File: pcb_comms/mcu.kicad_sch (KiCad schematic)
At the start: 34 parts, among them U3 STM32WLE5CCU6, Y1 32.768KHz, Y2 32MHz

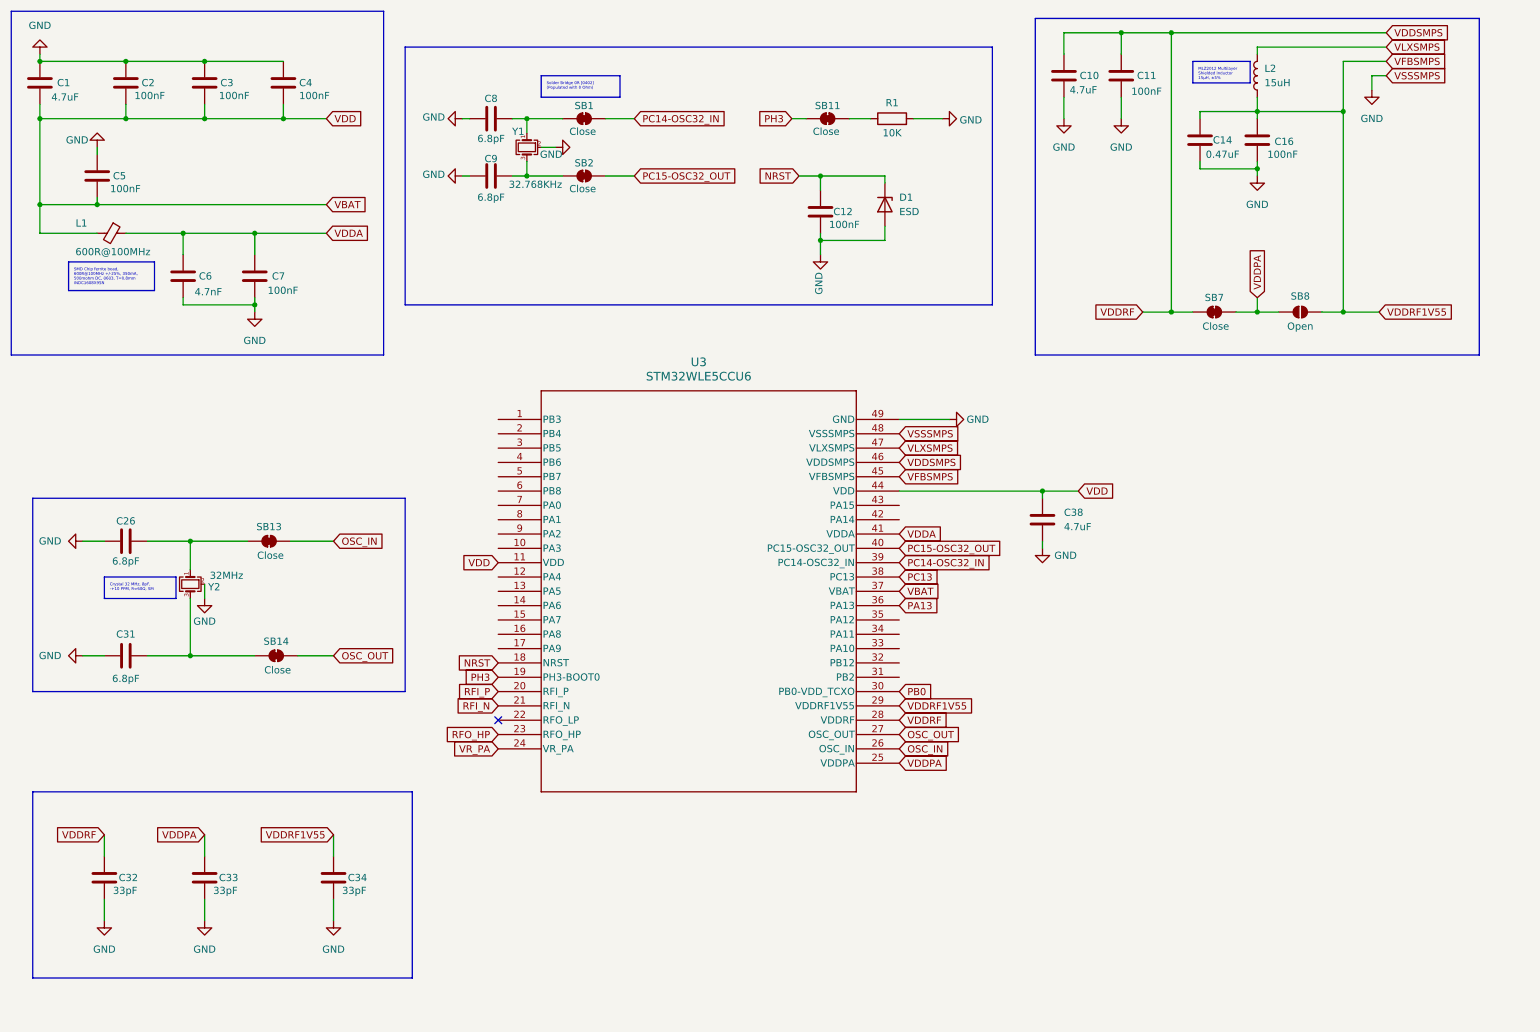
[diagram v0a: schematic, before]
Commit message: Add usb and gps
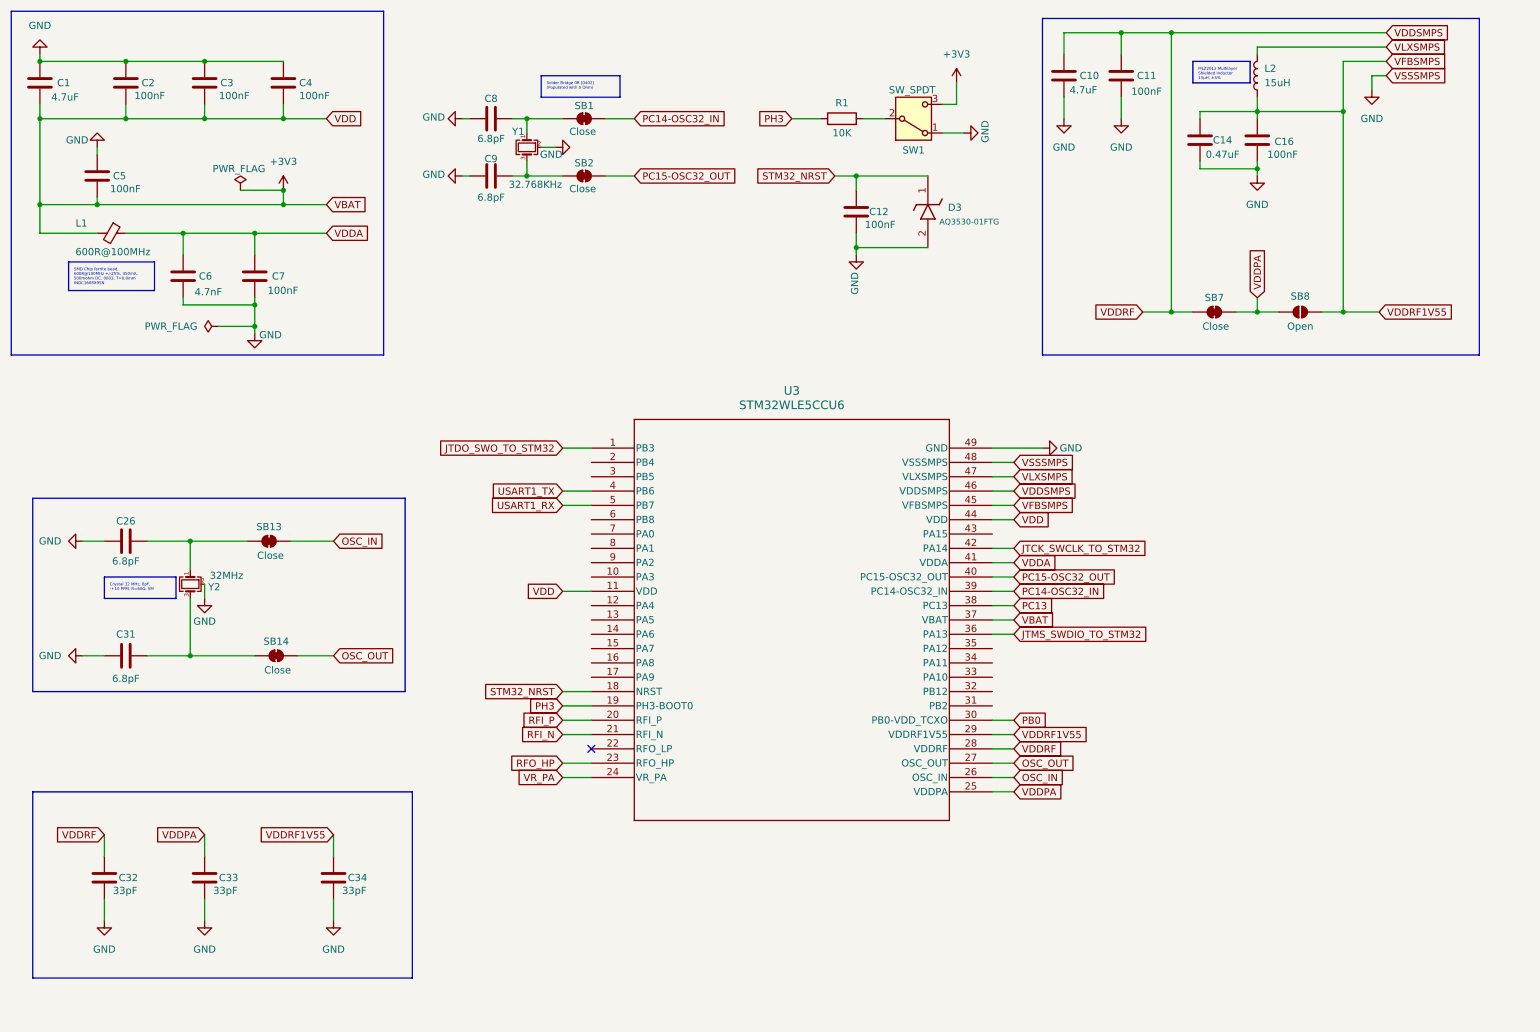
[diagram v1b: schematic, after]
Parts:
- removed C38: 4.7uF, symbol Device:C
- removed D1: ESD, symbol Diode:ESD5Zxx
- removed SB11: Close, symbol Jumper:SolderJumper_2_Bridged
- added D3: AQ3530-01FTG, symbol ESD_PROTECTION_DIODE_AQ3530-01FTG:AQ3530-01FTG
- added SW1: SW_SPDT, symbol Switch:SW_SPDT
- U3: footprint UFQFPN48_STM -> (none)
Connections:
- net GND: now also D3.2 (A), SW1.1 (A); no longer R1.2
- net PH3: now also R1.1
- net JTDO_SWO_TO_STM32: now reaches U3.1 (PB3)
- net USART1_TX: now reaches U3.4 (PB6)
- net JTCK_SWCLK_TO_STM32: now reaches U3.42 (PA14)
- net USART1_RX: now reaches U3.5 (PB7)
- net NRST renamed STM32_NRST
- net STM32_NRST: now also D3.1 (K)
- net PA13 renamed JTMS_SWDIO_TO_STM32
- net VBAT renamed +3V3
- net +3V3: now also SW1.3 (C)
- new net: R1.2, SW1.2 (B)
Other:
- moved on the sheet: C12, R1, U3

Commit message: Update GPS
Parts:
- removed SB1, SB13, SB14, SB2: Close, symbol Jumper:SolderJumper_2_Bridged
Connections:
- net OSC_IN is gone; now on net STM32_OSC_IN: U3.26 (OSC_IN)
- net OSC_OUT is gone; now on net STM32_OSC_OUT: U3.27 (OSC_OUT)
- net PC14-OSC32_IN is gone; now on net STM32_OSC_RTC_IN: U3.39 (PC14-OSC32_IN)
- net PC15-OSC32_OUT is gone; now on net STM32_OSC_RTC_OUT: U3.40 (PC15-OSC32_OUT)
- net STM32_OSC_IN: now reaches C26.2, Y2.1
- net MAX_TXO_TO_STM32: now reaches U3.10 (PA3)
- net MAX_PPS_TO_STM32: now reaches U3.12 (PA4)
- net MAX_SAFE_N_TO_STM32: now reaches U3.13 (PA5)
- net RF_CRL1_TO_STM32: now reaches U3.14 (PA6)
- net RF_CRL2_TO_STM32: now reaches U3.15 (PA7)
- net I2C1_SDA: now reaches U3.33 (PA10)
- net I2C1_SCL: now reaches U3.6 (PB8)
- net MAX_RESET_N_TO_STM32: now reaches U3.7 (PA0)
- net MAX_INT_TO_STM32: now reaches U3.8 (PA1)
- net MAX_RXI_TO_STM32: now reaches U3.9 (PA2)
- net STM32_OSC_RTC_OUT: now reaches C9.2, Y1.3
- net STM32_OSC_OUT: now reaches C31.2, Y2.3
- net STM32_OSC_RTC_IN: now reaches C8.2, Y1.1
- net PB0: no longer names the net of U3.30 (PB0-VDD_TCXO)
- net PC13: no longer names the net of U3.38 (PC13)
- net PH3 renamed STM32_BOOT
- no-connect marks 1 -> 12
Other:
- note added: "BOOT AND RESET"
- note added: "CLOCK"
- note added: "RTC"
- note added: "VDD Capacitors"
- note added: "VDDRF Capacitors"
- moved on the sheet: C1, C10, C11, C12, C14, C16, C2, C26, C3, C31, C32, C33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

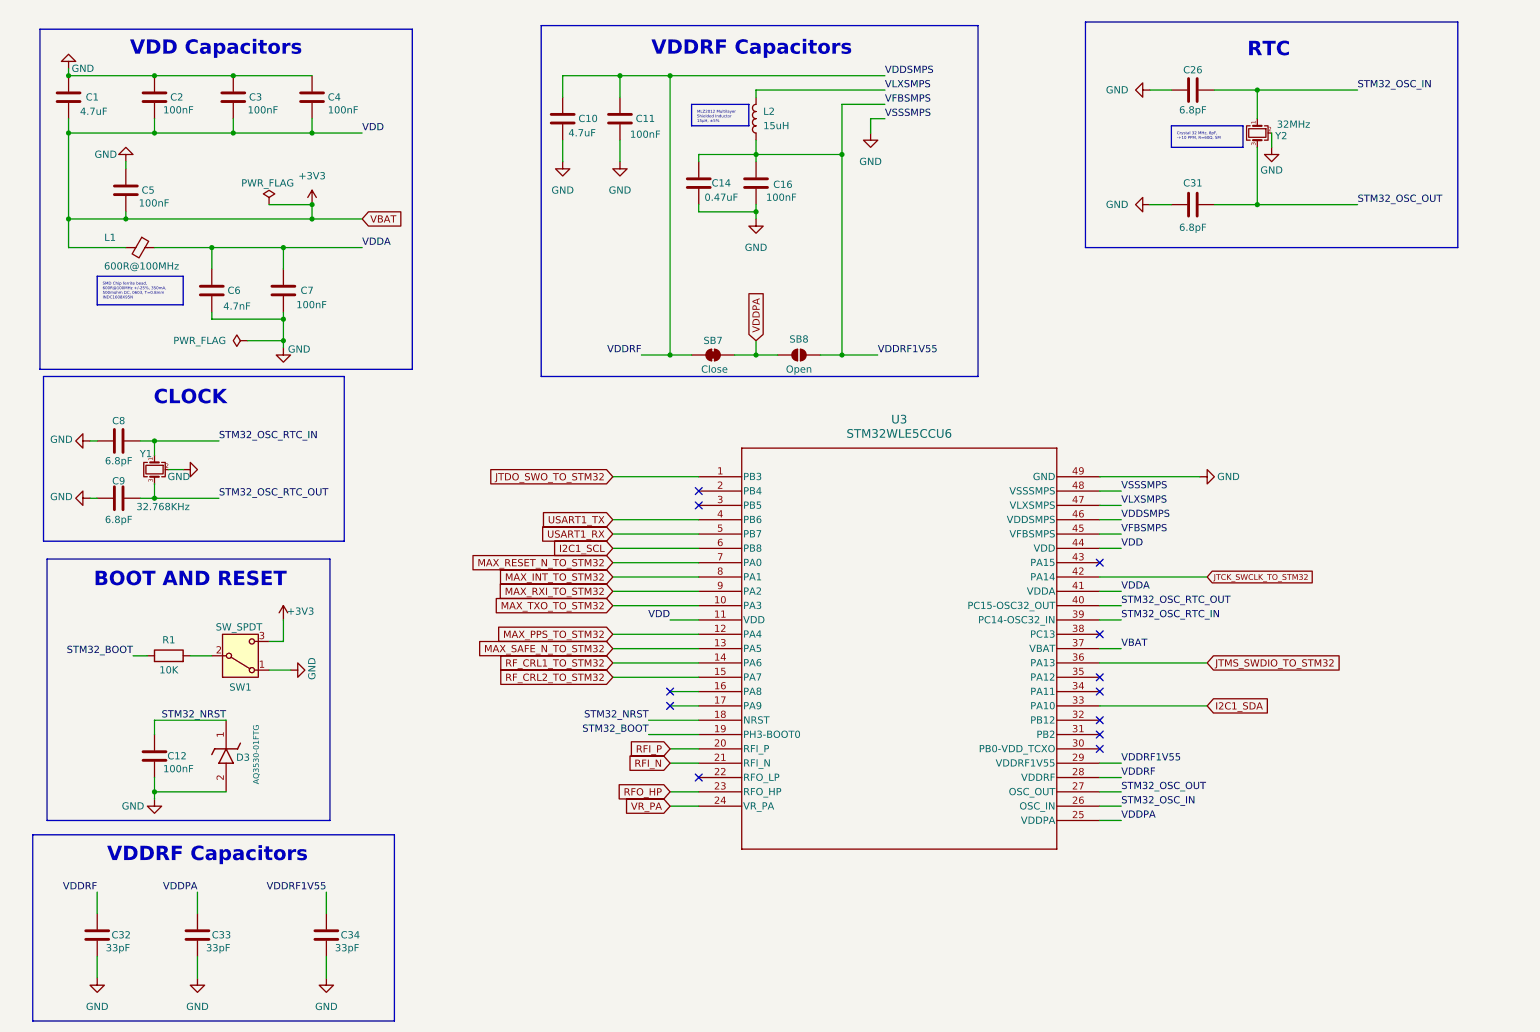
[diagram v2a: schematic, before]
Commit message: Add antenna deploy
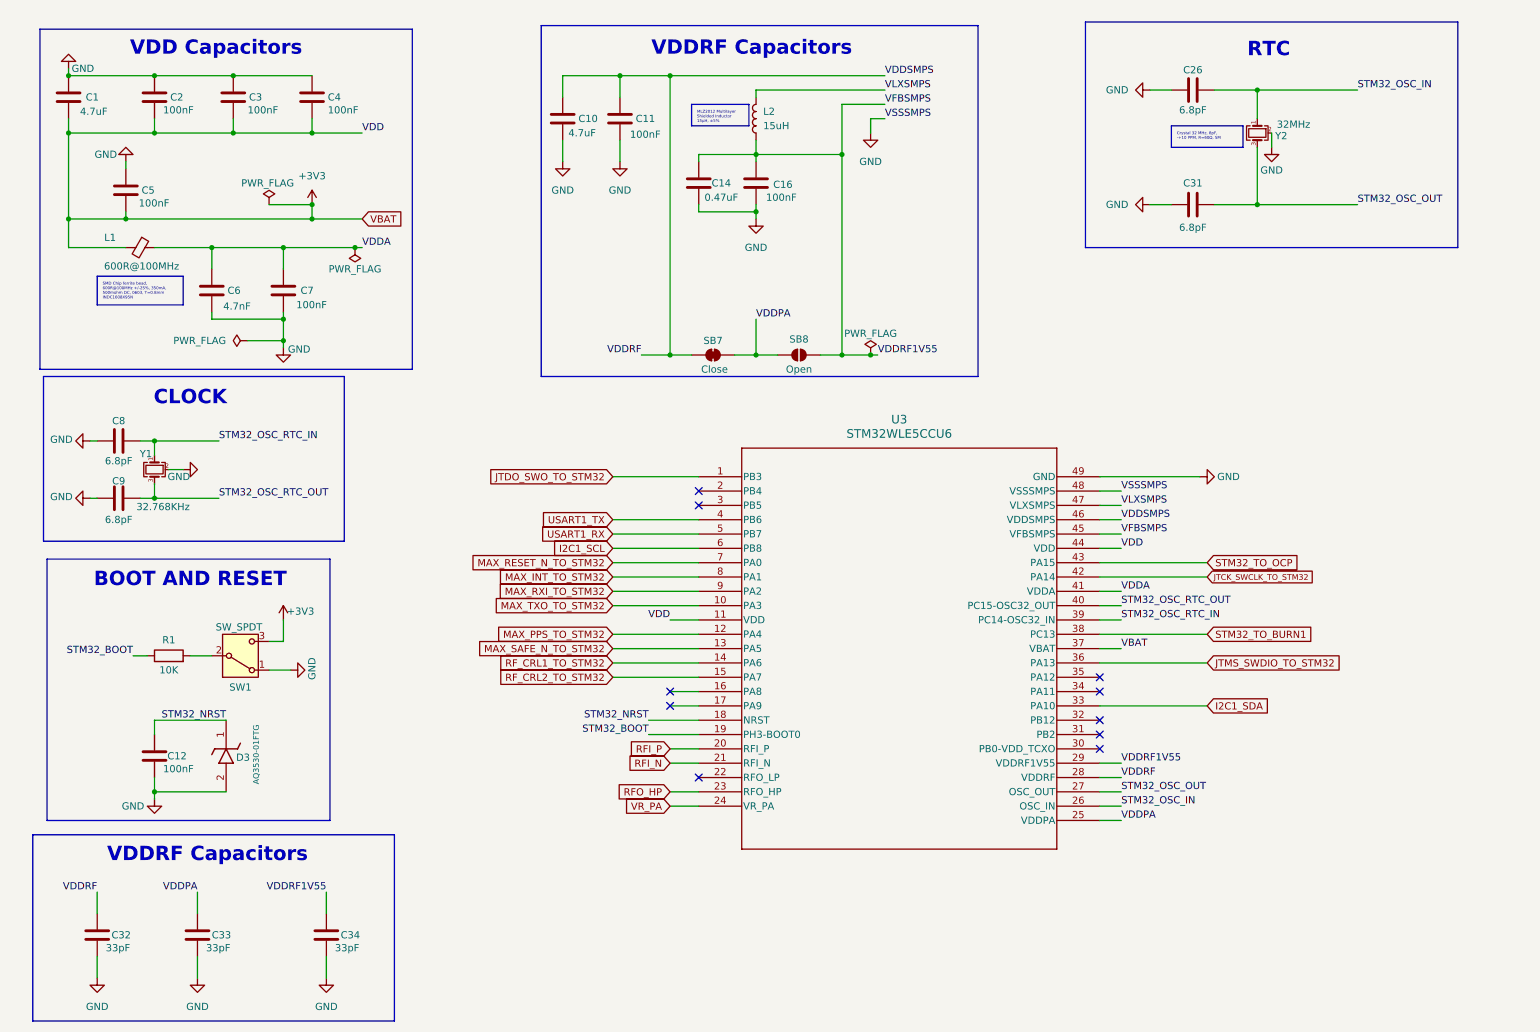
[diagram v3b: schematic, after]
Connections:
- net STM32_TO_BURN1: now reaches U3.38 (PC13)
- net STM32_TO_OCP: now reaches U3.43 (PA15)
- no-connect marks 12 -> 10
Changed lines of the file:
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@@
 	)
 	(junction
+		(at 76.2 57.15)
+		(diameter 0)
+		(color 0 0 0 0)
+	)
+	(junction
 		(at 147.32 50.8)
 		(diameter 0)
@@
 	)
 	(junction
+		(at 167.64 76.2)
+		(diameter 0)
+		(color 0 0 0 0)
+	)
+	(junction
 		(at 68.58 36.83)
 		(diameter 0)
@@
 	)
 	(no_connect
-		(at 208.28 125.73)
-	)
-	(no_connect
 		(at 208.28 140.97)
 	)
@@
 	)
 	(no_connect
-		(at 208.28 113.03)
-	)
-	(no_connect
 		(at 137.16 151.13)
 	)
@@
 	(wire
 		(pts
+			(xy 76.2 57.15) (xy 77.47 57.15)
+		)
+		(stroke
+			(width 0)
+			(type default)
+		)
+	)
+	(wire
+		(pts
 			(xy 143.51 76.2) (xy 147.32 76.2)
 		)
@@
 	(wire
 		(pts
-			(xy 63.5 57.15) (xy 77.47 57.15)
+			(xy 63.5 57.15) (xy 76.2 57.15)
 		)
 		(stroke
@@
 	(wire
 		(pts
+			(xy 167.64 76.2) (xy 168.91 76.2)
+		)
+		(stroke
+			(width 0)
+			(type default)
+		)
+	)
+	(wire
+		(pts
 			(xy 60.96 132.08) (xy 64.77 132.08)
 		)
@@
 	(wire
 		(pts
+			(xy 208.28 125.73) (xy 227.33 125.73)
+		)
+		(stroke
+			(width 0)
+			(type default)
+		)
+	)
+	(wire
+		(pts
 			(xy 170.18 31.75) (xy 162.56 31.75)
 		)
@@
 	(wire
 		(pts
-			(xy 162.56 76.2) (xy 168.91 76.2)
+			(xy 162.56 76.2) (xy 167.64 76.2)
 		)
 		(stroke
@@
 	(wire
 		(pts
-			(xy 147.32 73.66) (xy 147.32 76.2)
+			(xy 147.32 69.85) (xy 147.32 76.2)
 		)
 		(stroke
@@
 	(wire
 		(pts
+			(xy 208.28 113.03) (xy 227.33 113.03)
+		)
+		(stroke
+			(width 0)
+			(type default)
+		)
+	)
+	(wire
+		(pts
 			(xy 236.22 49.53) (xy 236.22 39.37)
 		)
@@
 		)
 	)
+	(label "VDDPA"
+		(at 147.32 69.85 0)
+		(effects
+			(font
+				(size 1.27 1.27)
+			)
+			(justify left bottom)
+		)
+	)
 	(label "VDDRF"
 		(at 127 76.2 180)
@@
 		)
 	)
+	(global_label "STM32_TO_OCP"
+		(shape input)
+		(at 227.33 113.03 0)
+		(fields_autoplaced yes)
+		(effects
+			(font
+				(size 1.27 1.27)
+			)
+			(justify left)
+		)
+		(property "Intersheetrefs" "${INTERSHEET_REFS}"
+			(at 244.4665 113.03 0)
+			(effects
+				(font
+					(size 1.27 1.27)
+				)
+				(justify left)
+				(hide yes)
+			)
+		)
+	)
 	(global_label "RF_CRL1_TO_STM32"
 		(shape input)
@@
 		)
 	)
-	(global_label "VDDPA"
+	(global_label "RFI_P"
 		(shape input)
-		(at 147.32 73.66 90)
+		(at 132.08 146.05 180)
 		(fields_autoplaced yes)
 		(effects
@@
 				(size 1.27 1.27)
 			)
-			(justify left)
+			(justify right)
 		)
 		(property "Intersheetrefs" "${INTERSHEET_REFS}"
-			(at 147.32 64.6876 90)
+			(at 123.8938 146.05 0)
 			(effects
 				(font
 					(size 1.27 1.27)
 				)
-				(justify left)
+				(justify right)
 				(hide yes)
 			)
 		)
 	)
-	(global_label "RFI_P"
+	(global_label "STM32_TO_BURN1"
 		(shape input)
-		(at 132.08 146.05 180)
+		(at 227.33 125.73 0)
 		(fields_autoplaced yes)
 		(effects
@@
 				(size 1.27 1.27)
 			)
-			(justify right)
+			(justify left)
 		)
 		(property "Intersheetrefs" "${INTERSHEET_REFS}"
-			(at 123.8938 146.05 0)
+			(at 247.0065 125.73 0)
 			(effects
 				(font
 					(size 1.27 1.27)
 				)
-				(justify right)
+				(justify left)
 				(hide yes)
 			)
@@
 	)
 	(symbol
+		(lib_id "power:PWR_FLAG")
+		(at 167.64 76.2 0)
+		(unit 1)
+		(exclude_from_sim no)
+		(in_bom yes)
+		(on_board yes)
+		(dnp no)
+		(property "Reference" "#FLG06"
+			(at 167.64 74.295 0)
+			(effects
+				(font
+					(size 1.27 1.27)
+				)
+				(hide yes)
+			)
+		)
+		(property "Value" "PWR_FLAG"
+			(at 167.64 72.39 0)
+			(effects
+				(font
+					(size 1.27 1.27)
+				)
+			)
+		)
+		(property "Footprint" ""
+			(at 167.64 76.2 0)
+			(effects
+				(font
+					(size 1.27 1.27)
+				)
+				(hide yes)
+			)
+		)
+		(property "Datasheet" "~"
+			(at 167.64 76.2 0)
+			(effects
+				(font
+					(size 1.27 1.27)
+				)
+				(hide yes)
+			)
+		)
+		(property "Description" "Special symbol for telling ERC where power comes from"
+			(at 167.64 76.2 0)
+			(effects
+				(font
+					(size 1.27 1.27)
+				)
+				(hide yes)
+			)
+		)
+		(pin "1"
+		)
+		(instances
+			(project "pcb_comms_board"
+				(path "/ea597178-b44d-4db9-826c-8f86e8d231f0/e138949f-a904-4d13-88f3-88172523fe12"
+					(reference "#FLG06")
+					(unit 1)
+				)
+			)
+		)
+	)
+	(symbol
 		(lib_id "power:GND")
 		(at 63.5 74.93 0)
@@
 					(unit 1)
 				)
+			)
+		)
+	)
+	(symbol
+		(lib_id "power:PWR_FLAG")
+		(at 76.2 57.15 0)
+		(mirror x)
+		(unit 1)
+		(exclude_from_sim no)
+		(in_bom yes)
+		(on_board yes)
+		(dnp no)
+		(property "Reference" "#FLG05"
+			(at 76.2 59.055 0)
+			(effects
+				(font
+					(size 1.27 1.27)
+				)
+				(hide yes)
+			)
+		)
+		(property "Value" "PWR_FLAG"
+			(at 76.2 60.96 0)
+			(effects
+				(font
+					(size 1.27 1.27)
+				)
+			)
+		)
+		(property "Footprint" ""
+			(at 76.2 57.15 0)
+			(effects
+				(font
+					(size 1.27 1.27)
+				)
+				(hide yes)
+			)
+		)
+		(property "Datasheet" "~"
+			(at 76.2 57.15 0)
+			(effects
+				(font
+					(size 1.27 1.27)
+				)
+				(hide yes)
+			)
+		)
+		(property "Description" "Special symbol for telling ERC where power comes from"
+			(at 76.2 57.15 0)
+			(effects
+				(font
+					(size 1.27 1.27)
+				)
+				(hide yes)
+			)
+		)
+		(pin "1"
+		)
+		(instances
+			(project ""
+				(path "/ea597178-b44d-4db9-826c-8f86e8d231f0/e138949f-a904-4d13-88f3-88172523fe12"
+					(reference "#FLG05")
+					(unit 1)
+				)
